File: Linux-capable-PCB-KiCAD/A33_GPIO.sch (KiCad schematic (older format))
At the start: 3 parts

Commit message: second push
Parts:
- added C?: 22u, symbol device:C
- added C? (x2): 100n, symbol device:C
- added C?: 1u, symbol device:C
- added C? (x2): 10u, symbol device:C
- added R? (x5): 100k, symbol device:R
- added R?: 10k, symbol device:R
- added R?: 200k, symbol device:R
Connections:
- net labels added: GND, SD_CLK, SD_CMD, SD_DAT0, SD_DAT1, SD_DAT2, SD_DAT3, SD_DET
- wire segments 0 -> 55
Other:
- moved on the sheet: U?D

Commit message: neki push
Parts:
- added C?: 100n, symbol device:C
- added C?: 10u, symbol device:C
- added C? (x2): 30p, symbol device:C
- added C? (x2): 10p, symbol device:C
- added J?: UART_CONN, symbol Connector:Conn_01x03_Male
- added J?: USB_A, symbol Connector:USB_A
- added Q?: Q_PMOS_GSD, symbol device:Q_PMOS_GSD
- added Q?: BC547, TO_SOT_Packages_THT:TO-92_Molded_Narrow, symbol Transistor:BC547
- added R?: 100k, symbol device:R
- added R? (x2): R, symbol device:R
- added R?: 10M, symbol device:R
- added TP?: Test_Point, symbol Connector:Test_Point
- added Y?: 24MHz, symbol device:Crystal_GND24
- added Y?: 32.768kHz, symbol device:Crystal
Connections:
- net labels added: +3V3, +5V, RESET, UART0_RX, UART0_TX, USB0-DN, USB0-DP, VBUS_~EN
- wire segments 55 -> 133

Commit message: od kuce
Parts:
- C? (x12): symbol device:C -> Linux-capable-PCB-KiCAD-rescue:C-device
- J?: symbol Connector:Micro_SD_Card_Det -> Linux-capable-PCB-KiCAD-rescue:Micro_SD_Card_Det-Connector
- Q?: symbol device:Q_PMOS_GSD -> Linux-capable-PCB-KiCAD-rescue:Q_PMOS_GSD-device
- Q?: symbol Transistor:BC547 -> Linux-capable-PCB-KiCAD-rescue:BC547-Transistor
- R? (x11): symbol device:R -> Linux-capable-PCB-KiCAD-rescue:R-device
- TP?: symbol Connector:Test_Point -> Linux-capable-PCB-KiCAD-rescue:Test_Point-Connector
- Y?: symbol device:Crystal_GND24 -> Linux-capable-PCB-KiCAD-rescue:Crystal_GND24-device
- Y?: symbol device:Crystal -> Linux-capable-PCB-KiCAD-rescue:Crystal-device
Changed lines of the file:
@@
 $Descr A4 11693 8268
 encoding utf-8
-Sheet 2 2
+Sheet 2 3
 Title ""
 Date ""
@@
 $EndComp
 $Comp
-L Connector:Micro_SD_Card_Det J?
+L Linux-capable-PCB-KiCAD-rescue:Micro_SD_Card_Det-Connector J?
 U 1 1 63014BA3
 P 10150 1500
+AR Path="/63014BA3" Ref="J?"  Part="1"
+AR Path="/62FC6136/63014BA3" Ref="J?"  Part="1"
 F 0 "J?" H 10100 2317 50  0000 C CNN
 F 1 "Micro_SD_Card_Det" H 10100 2226 50  0000 C CNN
@@
 $EndComp
 $Comp
-L device:R R?
+L Linux-capable-PCB-KiCAD-rescue:R-device R?
 U 1 1 62A8CA5B
 P 8600 1100
@@
 $EndComp
 $Comp
-L device:R R?
+L Linux-capable-PCB-KiCAD-rescue:R-device R?
 U 1 1 62A8DFC1
 P 8600 1200
@@
 $EndComp
 $Comp
-L device:R R?
+L Linux-capable-PCB-KiCAD-rescue:R-device R?
 U 1 1 62A8E139
 P 8600 1300
@@
 $EndComp
 $Comp
-L device:R R?
+L Linux-capable-PCB-KiCAD-rescue:R-device R?
 U 1 1 62A8E387
 P 8600 1900
@@
 $EndComp
 $Comp
-L device:R R?
+L Linux-capable-PCB-KiCAD-rescue:R-device R?
 U 1 1 62A8E9A0
 P 8600 1800
@@
 $EndComp
 $Comp
-L device:R R?
+L Linux-capable-PCB-KiCAD-rescue:R-device R?
 U 1 1 62A8EB5C
 P 8600 1700
@@
 $EndComp
 $Comp
-L device:C C?
+L Linux-capable-PCB-KiCAD-rescue:C-device C?
 U 1 1 62A90FA7
 P 7750 1300
@@
 $EndComp
 $Comp
-L device:C C?
+L Linux-capable-PCB-KiCAD-rescue:C-device C?
 U 1 1 62A9191B
 P 7300 1300
@@
 	11000 2000 11000 2100
 $Comp
-L device:C C?
+L Linux-capable-PCB-KiCAD-rescue:C-device C?
 U 1 1 62A9C7B1
 P 10350 5450
@@
 $EndComp
 $Comp
-L device:C C?
+L Linux-capable-PCB-KiCAD-rescue:C-device C?
 U 1 1 62A9E653
 P 10350 5650
@@
 $EndComp
 $Comp
-L device:C C?
+L Linux-capable-PCB-KiCAD-rescue:C-device C?
 U 1 1 62A9EA67
 P 10350 5950
@@
 $EndComp
 $Comp
-L device:C C?
+L Linux-capable-PCB-KiCAD-rescue:C-device C?
 U 1 1 62A9EF50
 P 10350 6150
@@
 $EndComp
 $Comp
-L device:R R?
+L Linux-capable-PCB-KiCAD-rescue:R-device R?
 U 1 1 62AA4C81
 P 10750 5800
@@
 USB0-DN
 $Comp
-L device:Q_PMOS_GSD Q?
+L Linux-capable-PCB-KiCAD-rescue:Q_PMOS_GSD-device Q?
 U 1 1 62AC1CE3
 P 6500 1900
@@
 	6400 2550 6250 2550
 $Comp
-L Transistor:BC547 Q?
+L Linux-capable-PCB-KiCAD-rescue:BC547-Transistor Q?
 U 1 1 62ACAA1B
 P 7050 2200
@@
 	6950 2400 6950 2500
 $Comp
-L device:R R?
+L Linux-capable-PCB-KiCAD-rescue:R-device R?
 U 1 1 62AD5055
 P 6950 1600
@@
 Connection ~ 11000 5650
 $Comp
-L device:C C?
+L Linux-capable-PCB-KiCAD-rescue:C-device C?
 U 1 1 62AE636B
 P 8000 5400
@@
 	8000 5550 8000 5750
 $Comp
-L device:R R?
+L Linux-capable-PCB-KiCAD-rescue:R-device R?
 U 1 1 62AEA37A
 P 7600 5150
@@
 $EndComp
 $Comp
-L device:R R?
+L Linux-capable-PCB-KiCAD-rescue:R-device R?
 U 1 1 62AEAD76
 P 7600 5050
@@
 RESET
 $Comp
-L Connector:Test_Point TP?
+L Linux-capable-PCB-KiCAD-rescue:Test_Point-Connector TP?
 U 1 1 62AFE911
 P 6900 5400
@@
 	6900 5500 6900 5400
 $Comp
-L device:C C?
+L Linux-capable-PCB-KiCAD-rescue:C-device C?
 U 1 1 62B03222
 P 8000 4650
@@
 	7700 4650 7850 4650
 $Comp
-L device:Crystal_GND24 Y?
+L Linux-capable-PCB-KiCAD-rescue:Crystal_GND24-device Y?
 U 1 1 62B0D565
 P 6050 4850
@@
 	6050 5000 6050 5150
 $Comp
-L device:C C?
+L Linux-capable-PCB-KiCAD-rescue:C-device C?
 U 1 1 62B2A956
 P 5200 4600
@@
 $EndComp
 $Comp
-L device:C C?
+L Linux-capable-PCB-KiCAD-rescue:C-device C?
 U 1 1 62B2B958
 P 5200 5150
@@
 	4850 5150 5050 5150
 $Comp
-L device:Crystal Y?
+L Linux-capable-PCB-KiCAD-rescue:Crystal-device Y?
 U 1 1 62B3E737
 P 6850 3850
@@
 	6750 4850 8300 4850
 $Comp
-L device:R R?
+L Linux-capable-PCB-KiCAD-rescue:R-device R?
 U 1 1 62B44DD9
 P 7450 3850
@@
 $EndComp
 $Comp
-L device:C C?
+L Linux-capable-PCB-KiCAD-rescue:C-device C?
 U 1 1 62B459A8
 P 6550 3500
@@
 $EndComp
 $Comp
-L device:C C?
+L Linux-capable-PCB-KiCAD-rescue:C-device C?
 U 1 1 62B461E0
 P 6550 4200
@@
 Wire Wire Line
 	6300 4200 6300 4300
+$Sheet
+S 4125 6000 975  750
+U 62B6FA43
+F0 "WiFi_chip" 50
+F1 "WiFi_chip.sch" 50
+$EndSheet
 $EndSCHEMATC

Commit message: Added some documents
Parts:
- added AE?: Antenna_Dipole, symbol device:Antenna_Dipole
- added U?: MIPI_DSI_Raspberry, symbol MIPI_DSI_Raspberry:MIPI_DSI_Raspberry
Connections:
- net labels added: SD_D0, SD_D1, SD_D2, SD_D3, WIFI_EN
- wire segments 133 -> 163
- no-connect marks 0 -> 16
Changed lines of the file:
@@
 	6300 4200 6300 4300
 $Sheet
-S 4125 6000 975  750
+S 4675 5950 975  750
 U 62B6FA43
 F0 "WiFi_chip" 50
 F1 "WiFi_chip.sch" 50
+F2 "SD_D1" I L 4675 6100 50
+F3 "SD_D0" I L 4675 6200 50
+F4 "SD_CLK" I L 4675 6300 50
+F5 "SD_CMD" I L 4675 6400 50
+F6 "SD_D3" I L 4675 6500 50
+F7 "SD_D2" I L 4675 6600 50
+F8 "WIFI_ANT" I R 5650 6100 50
+F9 "WIFI_EN" I R 5650 6200 50
+F10 "VDD33" I R 5650 6300 50
+F11 "VDIO" I R 5650 6400 50
 $EndSheet
+Wire Wire Line
+	4675 6100 4425 6100
+Wire Wire Line
+	4675 6200 4425 6200
+Wire Wire Line
+	4675 6300 4425 6300
+Wire Wire Line
+	4675 6400 4425 6400
+Wire Wire Line
+	4675 6500 4425 6500
+Wire Wire Line
+	4675 6600 4425 6600
+Wire Wire Line
+	5650 6100 5875 6100
+Wire Wire Line
+	5650 6200 5875 6200
+Text Label 4425 6100 2    50   ~ 0
+SD_D1
+Text Label 4425 6200 2    50   ~ 0
+SD_D0
+Text Label 4425 6300 2    50   ~ 0
+SD_CLK
+Text Label 4425 6400 2    50   ~ 0
+SD_CMD
+Text Label 4425 6500 2    50   ~ 0
+SD_D3
+Text Label 4425 6600 2    50   ~ 0
+SD_D2
+Text Label 5875 6200 0    50   ~ 0
+WIFI_EN
+Wire Wire Line
+	2150 3600 2400 3600
+Wire Wire Line
+	2150 3700 2400 3700
+Wire Wire Line
+	2150 3800 2400 3800
+Wire Wire Line
+	2150 3900 2400 3900
+Wire Wire Line
+	2150 4000 2400 4000
+Wire Wire Line
+	2150 4100 2400 4100
+Text Label 2400 3600 0    50   ~ 0
+SD_D1
+Text Label 2400 3700 0    50   ~ 0
+SD_D0
+Text Label 2400 3800 0    50   ~ 0
+SD_CLK
+Text Label 2400 3900 0    50   ~ 0
+SD_CMD
+Text Label 2400 4000 0    50   ~ 0
+SD_D3
+Text Label 2400 4100 0    50   ~ 0
+SD_D2
+Wire Wire Line
+	2150 4200 2400 4200
+Text Label 2400 4200 0    50   ~ 0
+WIFI_EN
+$Comp
+L power:+3V3 #PWR?
+U 1 1 62BC8F49
+P 6400 6275
+F 0 "#PWR?" H 6400 6125 50  0001 C CNN
+F 1 "+3V3" H 6415 6448 50  0000 C CNN
+F 2 "" H 6400 6275 50  0001 C CNN
+F 3 "" H 6400 6275 50  0001 C CNN
+	1    6400 6275
+	1    0    0    -1
+$EndComp
+Wire Wire Line
+	6400 6300 6400 6275
+Wire Wire Line
+	5650 6300 6400 6300
+Wire Wire Line
+	6400 6400 6400 6300
+Wire Wire Line
+	5650 6400 6400 6400
+Connection ~ 6400 6300
+$Comp
+L device:Antenna_Dipole AE?
+U 1 1 62BDE556
+P 5875 5550
+F 0 "AE?" H 6105 5464 50  0000 L CNN
+F 1 "Antenna_Dipole" H 6105 5373 50  0000 L CNN
+F 2 "" H 5875 5550 50  0001 C CNN
+F 3 "" H 5875 5550 50  0001 C CNN
+	1    5875 5550
+	1    0    0    -1
+$EndComp
+Wire Wire Line
+	5875 5750 5875 6100
+$Comp
+L power:GND #PWR?
+U 1 1 62BE7FC5
+P 5975 5875
+F 0 "#PWR?" H 5975 5625 50  0001 C CNN
+F 1 "GND" H 5980 5702 50  0000 C CNN
+F 2 "" H 5975 5875 50  0001 C CNN
+F 3 "" H 5975 5875 50  0001 C CNN
+	1    5975 5875
+	1    0    0    -1
+$EndComp
+Wire Wire Line
+	5975 5875 5975 5750
+$Comp
+L MIPI_DSI_Raspberry:MIPI_DSI_Raspberry U?
+U 1 1 62BF49A5
+P 4775 1850
+F 0 "U?" H 4750 2865 50  0000 C CNN
+F 1 "MIPI_DSI_Raspberry" H 4750 2774 50  0000 C CNN
+F 2 "" H 4775 1850 50  0001 C CNN
+F 3 "" H 4775 1850 50  0001 C CNN
+	1    4775 1850
+	1    0    0    -1
+$EndComp
+NoConn ~ 5175 1100
+NoConn ~ 5175 1200
+NoConn ~ 5175 1300
+NoConn ~ 5175 1400
+NoConn ~ 5175 1500
+NoConn ~ 5175 1600
+NoConn ~ 5175 1700
+NoConn ~ 5175 1800
+NoConn ~ 5175 1900
+NoConn ~ 5175 2000
+NoConn ~ 5175 2100
+NoConn ~ 5175 2200
+NoConn ~ 5175 2300
+NoConn ~ 5175 2400
+NoConn ~ 5175 2500
+Wire Wire Line
+	4325 1100 4225 1100
+Wire Wire Line
+	4225 1100 4225 1400
+$Comp
+L power:GND #PWR?
+U 1 1 62C7BB53
+P 4225 2600
+F 0 "#PWR?" H 4225 2350 50  0001 C CNN
+F 1 "GND" H 4230 2427 50  0000 C CNN
+F 2 "" H 4225 2600 50  0001 C CNN
+F 3 "" H 4225 2600 50  0001 C CNN
+	1    4225 2600
+	1    0    0    -1
+$EndComp
+Wire Wire Line
+	4325 1400 4225 1400
+Connection ~ 4225 1400
+Wire Wire Line
+	4225 1400 4225 1700
+Wire Wire Line
+	4325 1700 4225 1700
+Connection ~ 4225 1700
+Wire Wire Line
+	4225 1700 4225 2000
+Wire Wire Line
+	4325 2000 4225 2000
+Connection ~ 4225 2000
+Wire Wire Line
+	4225 2000 4225 2600
+NoConn ~ 4325 2200
+$Comp
+L power:+3V3 #PWR?
+U 1 1 62CB19B6
+P 3300 2500
+F 0 "#PWR?" H 3300 2350 50  0001 C CNN
+F 1 "+3V3" H 3315 2673 50  0000 C CNN
+F 2 "" H 3300 2500 50  0001 C CNN
+F 3 "" H 3300 2500 50  0001 C CNN
+	1    3300 2500
+	1    0    0    -1
+$EndComp
+Wire Wire Line
+	3300 2500 4325 2500
 $EndSCHEMATC

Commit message: RAM cip je spojen
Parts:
- AE?: symbol device:Antenna_Dipole -> Linux-capable-PCB-KiCAD-rescue:Antenna_Dipole-device
- J?: symbol Connector:USB_A -> Linux-capable-PCB-KiCAD-rescue:USB_A-Connector
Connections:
- wire segments 163 -> 164
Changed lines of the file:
@@
 $Descr A4 11693 8268
 encoding utf-8
-Sheet 2 3
+Sheet 2 4
 Title ""
 Date ""
@@
 U 1 1 62AA4C81
 P 10750 5800
-F 0 "R?" V 10750 5800 50  0000 C CNN
-F 1 "200k" V 10700 5600 50  0000 C CNN
+F 0 "R?" V 10700 5575 50  0000 C CNN
+F 1 "200k" V 10750 5800 50  0000 C CNN
 F 2 "" V 10680 5800 50  0001 C CNN
 F 3 "" H 10750 5800 50  0001 C CNN
@@
 Wire Wire Line
 	11000 5800 11000 5950
-Wire Wire Line
-	10100 5800 10100 5950
-Wire Wire Line
-	10100 6150 10200 6150
-Connection ~ 10100 5800
-Wire Wire Line
-	10100 5950 10200 5950
-Connection ~ 10100 5950
-Wire Wire Line
-	10100 5950 10100 6150
 Wire Wire Line
 	10500 5950 11000 5950
@@
 	1100 1550 1100 1400
 $Comp
-L Connector:USB_A J?
+L Linux-capable-PCB-KiCAD-rescue:USB_A-Connector J?
 U 1 1 62AB417B
 P 5950 2750
+AR Path="/62AB417B" Ref="J?"  Part="1"
+AR Path="/62FC6136/62AB417B" Ref="J?"  Part="1"
 F 0 "J?" H 6007 3217 50  0000 C CNN
 F 1 "USB_A" H 6007 3126 50  0000 C CNN
@@
 Connection ~ 6400 6300
 $Comp
-L device:Antenna_Dipole AE?
+L Linux-capable-PCB-KiCAD-rescue:Antenna_Dipole-device AE?
 U 1 1 62BDE556
 P 5875 5550
@@
 Wire Wire Line
 	3300 2500 4325 2500
+Wire Wire Line
+	9900 5650 10000 5650
+Wire Wire Line
+	10000 5650 10000 5950
+Wire Wire Line
+	10000 5950 10200 5950
+Wire Wire Line
+	10000 5950 10000 6150
+Wire Wire Line
+	10000 6150 10200 6150
+Connection ~ 10000 5950
 $EndSCHEMATC

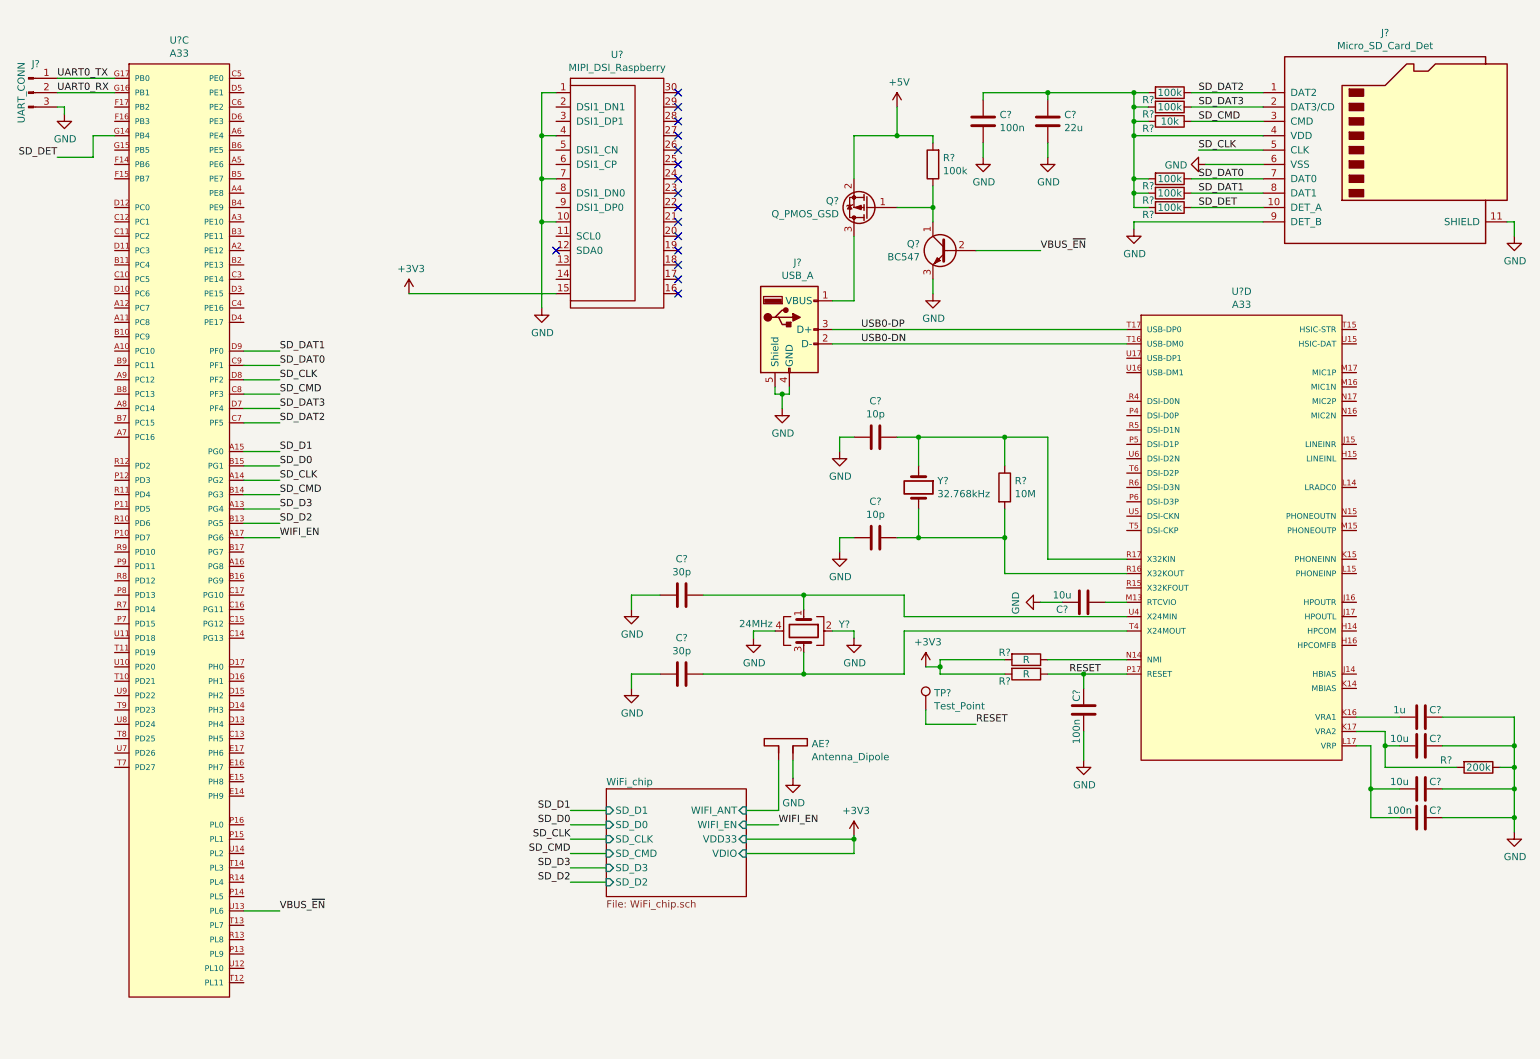
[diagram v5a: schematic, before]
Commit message: added ESD protection, g sensor
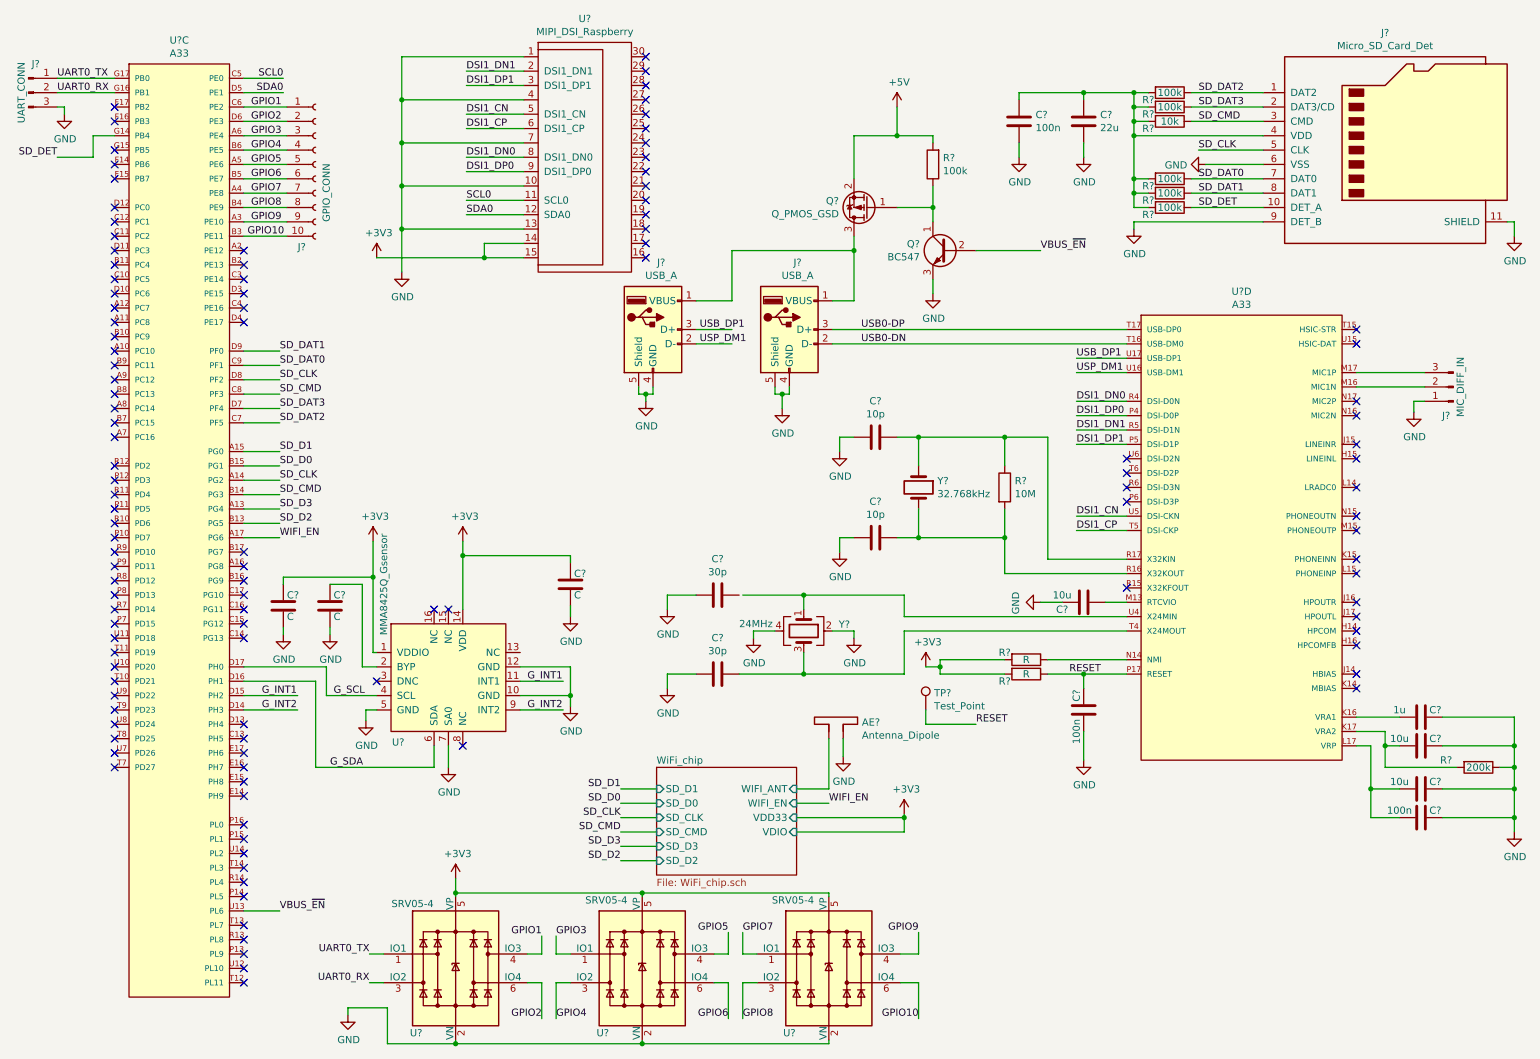
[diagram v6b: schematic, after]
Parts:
- added C? (x3): C, symbol Device:C
- added J?: GPIO_CONN, symbol Connector:Conn_01x10_Female
- added J?: USB_A, symbol Linux-capable-PCB-KiCAD-rescue:USB_A-Connector
- added J?: MIC_DIFF_IN, symbol Connector:Conn_01x03_Male
- added U?: MMA8425Q_Gsensor, symbol MMA8425Q_Gsensor:MMA8425Q_Gsensor
- added U? (x3): SRV05-4, Package_TO_SOT_SMD:SOT-23-6, symbol Power_Protection:SRV05-4
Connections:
- net +3V3: now also U?.14, C?.1, C?.1, U?.1 (VDDIO), U?.14 (VDD), U?.5 (VP), U?.5 (VP), U?.5 (VP)
- net GND: now also U?.13, C?.2, C?.2, C?.2, J?.1 (Pin_1), J?.4 (GND), J?.5 (Shield), U?.10 (GND), U?.12 (GND), U?.2 (VN), U?.2 (VN), U?.2 (VN), U?.5 (GND), U?.7 (SA0)
- net UART0_RX: now also U?.3 (IO2)
- net UART0_TX: now also U?.1 (IO1)
- net at J?.1 (VBUS), Q?.3 (D): now also J?.1 (VBUS)
- net at U?.U4 (X24MIN), Y?.1: no longer C?.1
- net SCL0: now reaches U?.11 (SCL0)
- net SCL0: now also U?.C5 (PE0)
- net SDA0: now reaches U?.12 (SDA0)
- net SDA0: now also U?.D5 (PE1)
- net DSI1_DN1: now reaches U?.2 (DSI1_DN1)
- net DSI1_DN1: now also U?.R5 (DSI-D1N)
- net DSI1_DP1: now reaches U?.3 (DSI1_DP1)
- net DSI1_DP1: now also U?.P5 (DSI-D1P)
- net DSI1_CN: now reaches U?.5 (DSI1_CN)
- net DSI1_CN: now also U?.U5 (DSI-CKN)
- net DSI1_CP: now reaches U?.6 (DSI1_CP)
- net DSI1_CP: now also U?.T5 (DSI-CKP)
- net DSI1_DN0: now reaches U?.8 (DSI1_DN0)
- net DSI1_DN0: now also U?.R4 (DSI-D0N)
- net DSI1_DP0: now reaches U?.9 (DSI1_DP0)
- net DSI1_DP0: now also U?.P4 (DSI-D0P)
- net GPIO9: now reaches U?.A3 (PE10)
- net GPIO9: now also J?.9 (Pin_9), U?.4 (IO3)
- net GPIO7: now reaches U?.A4 (PE8)
- net GPIO7: now also J?.7 (Pin_7), U?.1 (IO1)
- net GPIO5: now reaches U?.A5 (PE6)
- net GPIO5: now also J?.5 (Pin_5), U?.4 (IO3)
- net GPIO3: now reaches U?.A6 (PE4)
- net GPIO3: now also J?.3 (Pin_3), U?.1 (IO1)
- net GPIO10: now reaches U?.B3 (PE11)
- net GPIO10: now also J?.10 (Pin_10), U?.6 (IO4)
- net GPIO8: now reaches U?.B4 (PE9)
- net GPIO8: now also J?.8 (Pin_8), U?.3 (IO2)
- net GPIO6: now reaches U?.B5 (PE7)
- net GPIO6: now also J?.6 (Pin_6), U?.6 (IO4)
- net GPIO4: now reaches U?.B6 (PE5)
- net GPIO4: now also J?.4 (Pin_4), U?.3 (IO2)
- net GPIO1: now reaches U?.C6 (PE2)
- net GPIO1: now also J?.1 (Pin_1), U?.4 (IO3)
- net G_INT2: now reaches U?.D14 (PH3)
- net G_INT2: now also U?.9 (INT2)
- net G_INT1: now reaches U?.D15 (PH2)
- net G_INT1: now also U?.11 (INT1)
- net G_SDA: now reaches U?.D16 (PH1)
- net G_SDA: now also U?.6 (SDA)
- net G_SCL: now reaches U?.D17 (PH0)
- net G_SCL: now also U?.4 (SCL)
- net GPIO2: now reaches U?.D6 (PE3)
- net GPIO2: now also J?.2 (Pin_2), U?.6 (IO4)
- net at U?.M16 (MIC1N): now also J?.2 (Pin_2)
- net at U?.M17 (MIC1P): now also J?.3 (Pin_3)
- net USP_DM1: now reaches U?.U16 (USB-DM1)
- net USP_DM1: now also J?.2 (D-)
- net USB_DP1: now reaches U?.U17 (USB-DP1)
- net USB_DP1: now also J?.3 (D+)
- new net: C?.1, U?.2 (BYP)
- no-connect marks 16 -> 115
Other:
- moved on the sheet: AE?, C?, U?

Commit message: Power supply schematics
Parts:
- C26, C27, C28: renamed from C?; symbol Device:C -> Linux-capable-PCB-KiCAD-rescue:C-Device
- U3, U5, U6: renamed from U?; symbol Power_Protection:SRV05-4 -> Linux-capable-PCB-KiCAD-rescue:SRV05-4-Power_Protection
- gave numbers to parts that had none: 38
